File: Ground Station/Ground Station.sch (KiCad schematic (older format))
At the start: 61 parts, among them IC1 ADP3335, IC2 STM32F042F6P6, IC3 Si4460, IC4 S25FL127S, J1 USB-PLUG, P1 SMA, P2 SWD_TC, X1 RF Frame, X2 RF Cover, X3 Casing, Y1 30MHz, Y2 26MHz

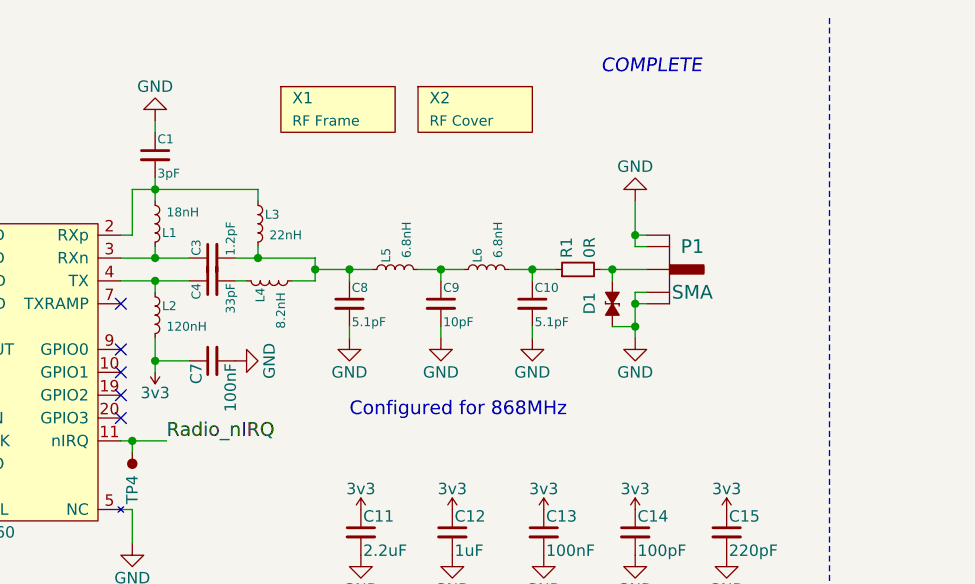
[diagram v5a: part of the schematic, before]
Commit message: Corrected Radio Passives in Ground Station
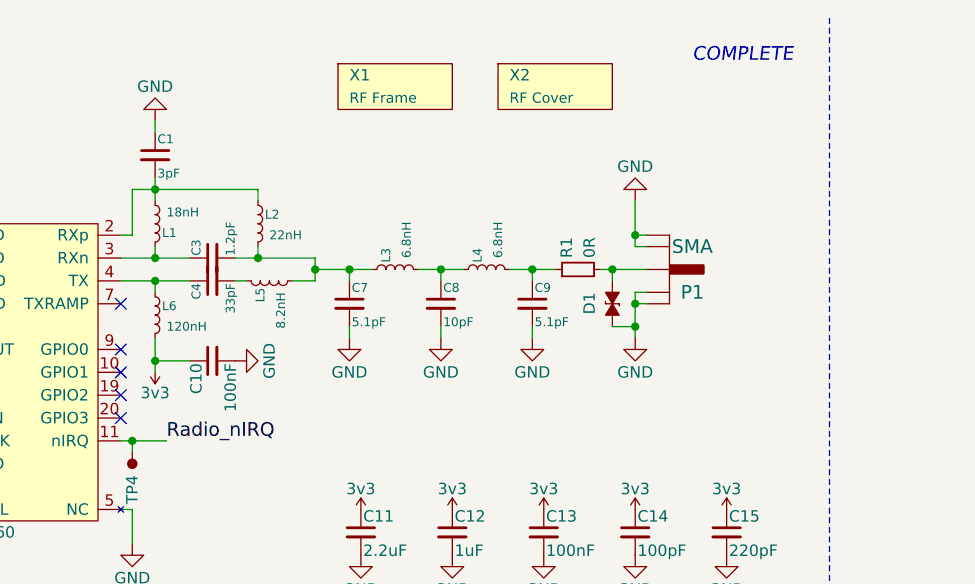
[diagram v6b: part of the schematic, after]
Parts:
- C10: value 5.1pF -> 100nF; Farnell 1885321 -> 1828860
- C7: value 100nF -> 5.1pF; Farnell 1828860 -> 1885321
- C8: value 5.1pF -> 10pF; Farnell 1885321 -> 1758941
- C9: value 10pF -> 5.1pF; Farnell 1758941 -> 1885321
- L2: value 120nH -> 22nH; footprint agg:0603-L -> agg:0402-L; Farnell 2424731 -> 1669580
- L3: value 22nH -> 6.8nH; Farnell 1669580 -> 1711736
- L4: value 8.2nH -> 6.8nH; Farnell 1865771 -> 1711736
- L5: value 6.8nH -> 8.2nH; Farnell 1711736 -> 1865771
- L6: value 6.8nH -> 120nH; footprint agg:0402-L -> agg:0603-L; Farnell 1711736 -> 2424731
- P1: footprint Library:SMA-142-0701-801 -> Library:SMA-J-P-H-ST-EM1; Farnell 1019325 -> (none); Samtec (none) -> SMA-J-P-H-ST-EM1
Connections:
- net 3v3: now also C10.1, L6.2; no longer C7.1, L2.2
- net at C1.2, IC3.2 (RXp), L1.2: now also L2.1; no longer L3.1
- net at C4.1, IC3.4 (TX): now also L6.1; no longer L2.1
- net at L4.1: now also C8.1, L3.2; no longer C4.2
- new net: C3.2, C7.1, L2.2, L3.1, L5.2
- new net: C4.2, L5.1
- new net: C9.1, L4.2, R1.1
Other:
- note removed: "Configured for 868MHz"

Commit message: Tidy up before final assembly
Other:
- note added: "Configured for 868MHz"
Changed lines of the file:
@@
 	1    0    0    -1
 $EndComp
+Text Notes 7250 2300 0    60   ~ 0
+Configured for 868MHz
 $EndSCHEMATC
